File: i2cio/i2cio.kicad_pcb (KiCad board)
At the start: 2 copper layers, 86.4 x 53.3 mm, 41 parts, among them CON1 BARREL_JACK, CON2 AVR-ISP-6, CON3 AVR-JTAG-10, IC1 ATMEGA32-A, P1 CONN_01X02, P10 CONN_01X03, P11 CONN_01X03, P4 CONN_01X11, P5 CONN_01X11, P6 CONN_01X11, P7 CONN_01X11, P8 CONN_02X08, SW1 Tactile_switch, U1 LM2940, U2 LM3940, U3 MCP4361, U4 MCP4361, U5 OPA4350, U6 OPA4350, Y1 16MHz

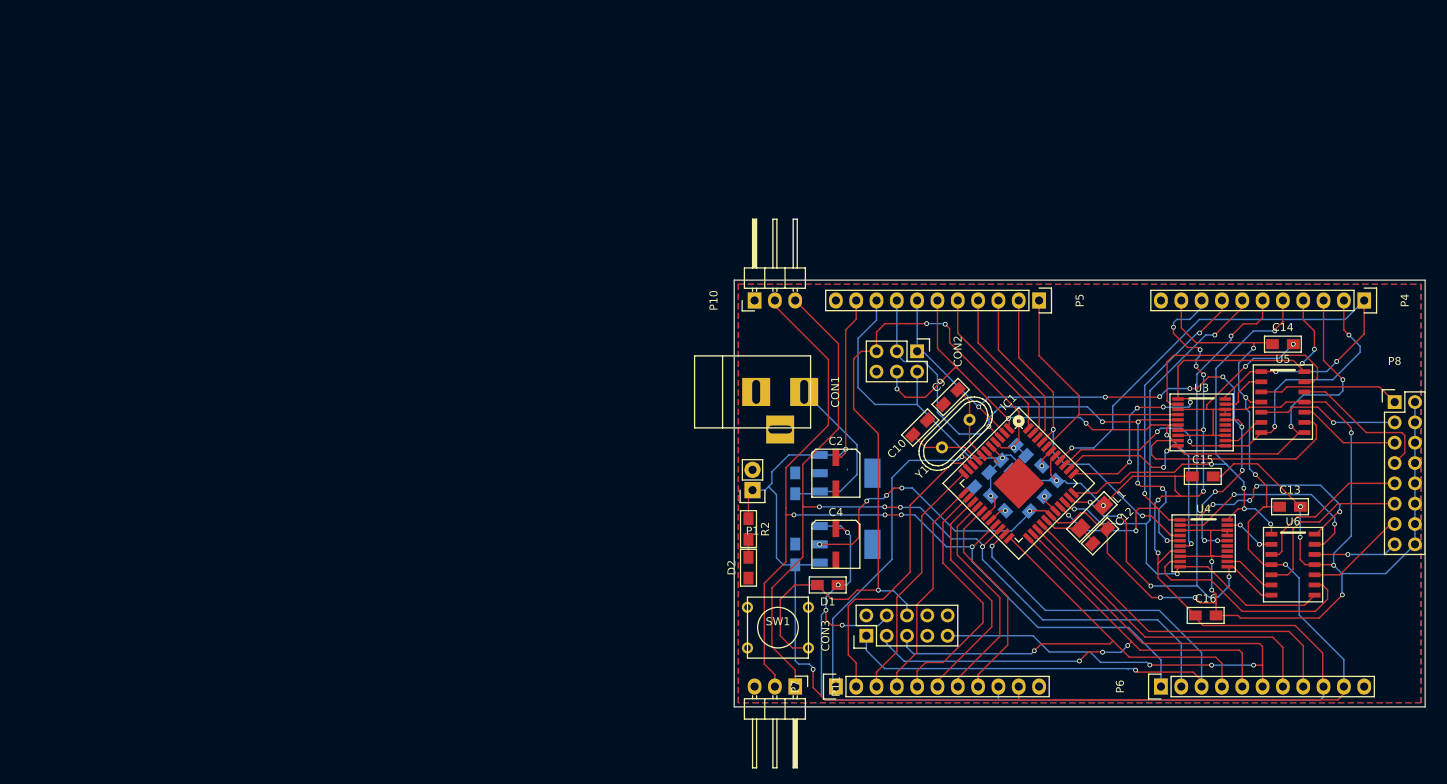
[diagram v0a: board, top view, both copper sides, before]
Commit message: onboarding the project to latest KiCad. Add 3d models for everything.
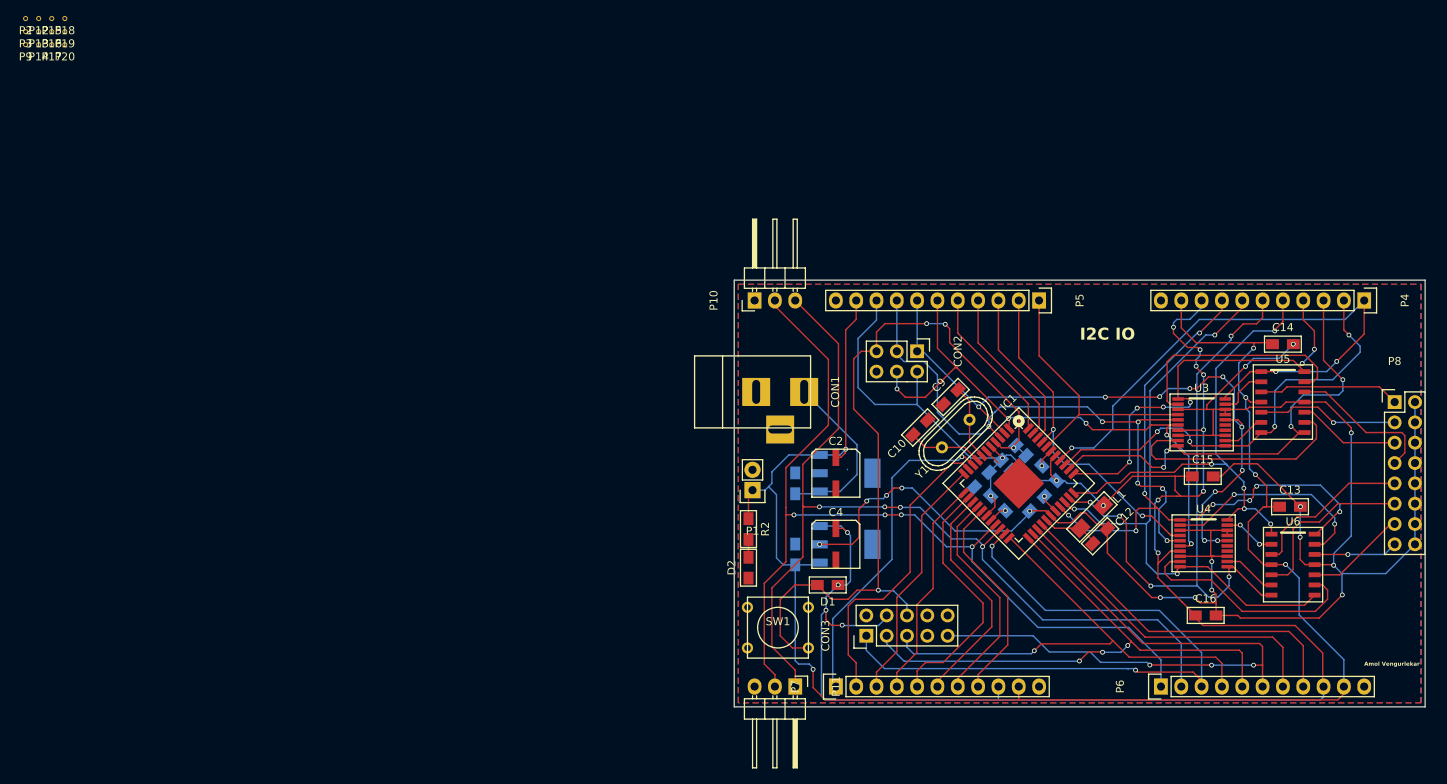
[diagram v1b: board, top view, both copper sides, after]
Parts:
- added P12: CONN_01X01, amol_parts_footprints:groundpoint, F.Cu at (1.95, 0.32)
- added P13: CONN_01X01, amol_parts_footprints:groundpoint, F.Cu at (1.95, 1.95)
- added P14: CONN_01X01, amol_parts_footprints:groundpoint, F.Cu at (1.95, 3.59)
- added P15: CONN_01X01, amol_parts_footprints:groundpoint, F.Cu at (3.59, 0.32)
- added P16: CONN_01X01, amol_parts_footprints:groundpoint, F.Cu at (3.59, 1.95)
- added P17: CONN_01X01, amol_parts_footprints:groundpoint, F.Cu at (3.59, 3.59)
- added P18: CONN_01X01, amol_parts_footprints:groundpoint, F.Cu at (5.22, 0.32)
- added P19: CONN_01X01, amol_parts_footprints:groundpoint, F.Cu at (5.22, 1.95)
- added P2: CONN_01X01, amol_parts_footprints:groundpoint, F.Cu at (0.32, 0.32)
- added P20: CONN_01X01, amol_parts_footprints:groundpoint, F.Cu at (5.22, 3.59)
- added P3: CONN_01X01, amol_parts_footprints:groundpoint, F.Cu at (0.32, 1.95)
- added P9: CONN_01X01, amol_parts_footprints:groundpoint, F.Cu at (0.32, 3.59)
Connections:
- net /AVR/~Reset renamed /AVR/~{Reset}
- CON1 pad 3: Net-(CON1-Pad3) -> unconnected-(CON1-Pad3)
- CON3 pad 7: Net-(CON3-Pad7) -> unconnected-(CON3-Pad7)
- CON3 pad 8: Net-(CON3-Pad8) -> unconnected-(CON3-Pad8)
- SW1 pad 1: Net-(SW1-Pad1) -> unconnected-(SW1-Pad1)
- SW1 pad 3: Net-(SW1-Pad3) -> unconnected-(SW1-Pad3)
- U3 pad 14: Net-(U3-Pad14) -> unconnected-(U3-~{WP}-Pad14)
- U3 pad 15: Net-(U3-Pad15) -> unconnected-(U3-~{RESET}-Pad15)
- U3 pad 19: Net-(U3-Pad19) -> PA2
- U4 pad 14: Net-(U4-Pad14) -> unconnected-(U4-~{WP}-Pad14)
- U4 pad 15: Net-(U4-Pad15) -> unconnected-(U4-~{RESET}-Pad15)
- U4 pad 19: Net-(U4-Pad19) -> PA6
- U5 pad 2: Net-(U3-Pad19) -> PA2
- U6 pad 2: Net-(U4-Pad19) -> PA6
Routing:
- net PA6: track 74.8 -> 81.3 mm, vias 3 -> 5
- net Net-(U4-Pad19): track 6.53 -> 0.00 mm, vias 2 -> 0
- net PA2: track 57.8 -> 64.1 mm
- net Net-(U3-Pad19): track 6.33 -> 0.00 mm
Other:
- net class Default removed
- board text added: "Amol Vengurlekar"
- board text added: "I2C IO"
